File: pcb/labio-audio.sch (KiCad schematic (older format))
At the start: 32 parts, among them J701 JACK_TRRS_6PINS, P701 CONN_01X04, P702 CONN_01X04, P703 CONN_01X04, P704 CONN_01X02, SW701 DIP_SWITCH_X04, SW702 DIP_SWITCH_X04, U701 SPU0410HR5H, U702 WM8750

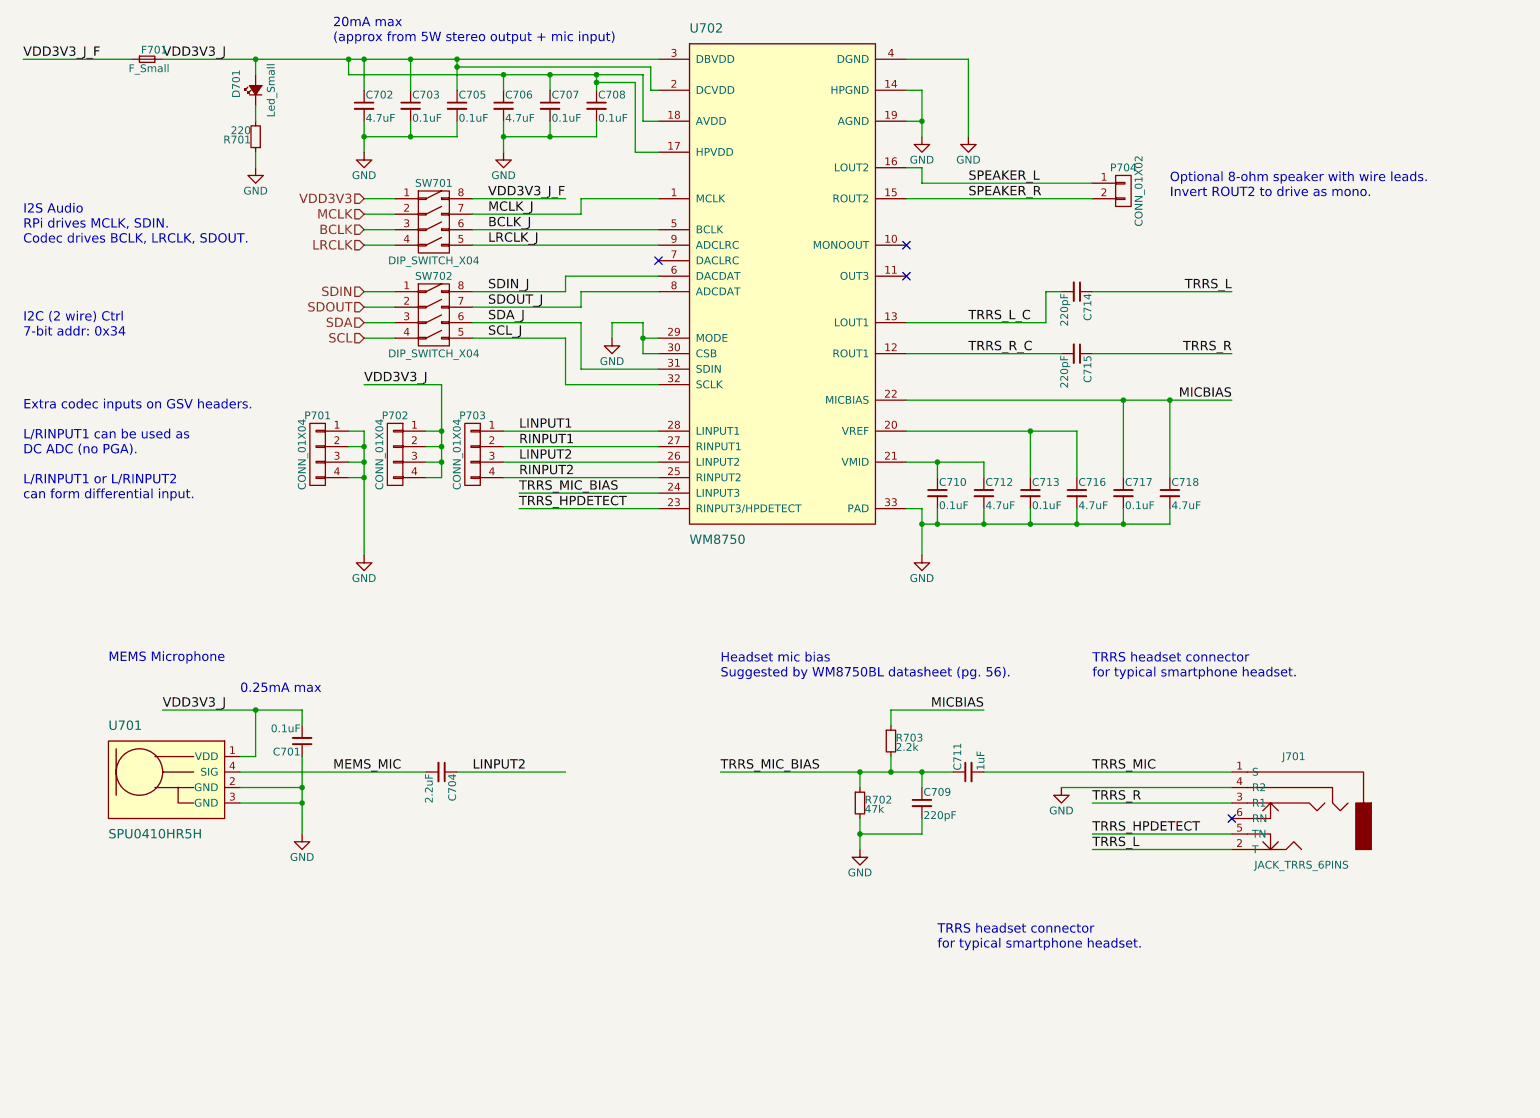
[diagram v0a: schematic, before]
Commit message: fix codec/mic/trrs bias circuit
* trrs (headset) mic bias was flipped (in vs out) from datasheet
* trrs l/r decoupling caps changed back to 220uF per datasheet and re-layout for 1210 ceramic
* mems mic decoupling changed to 1uF for consistency
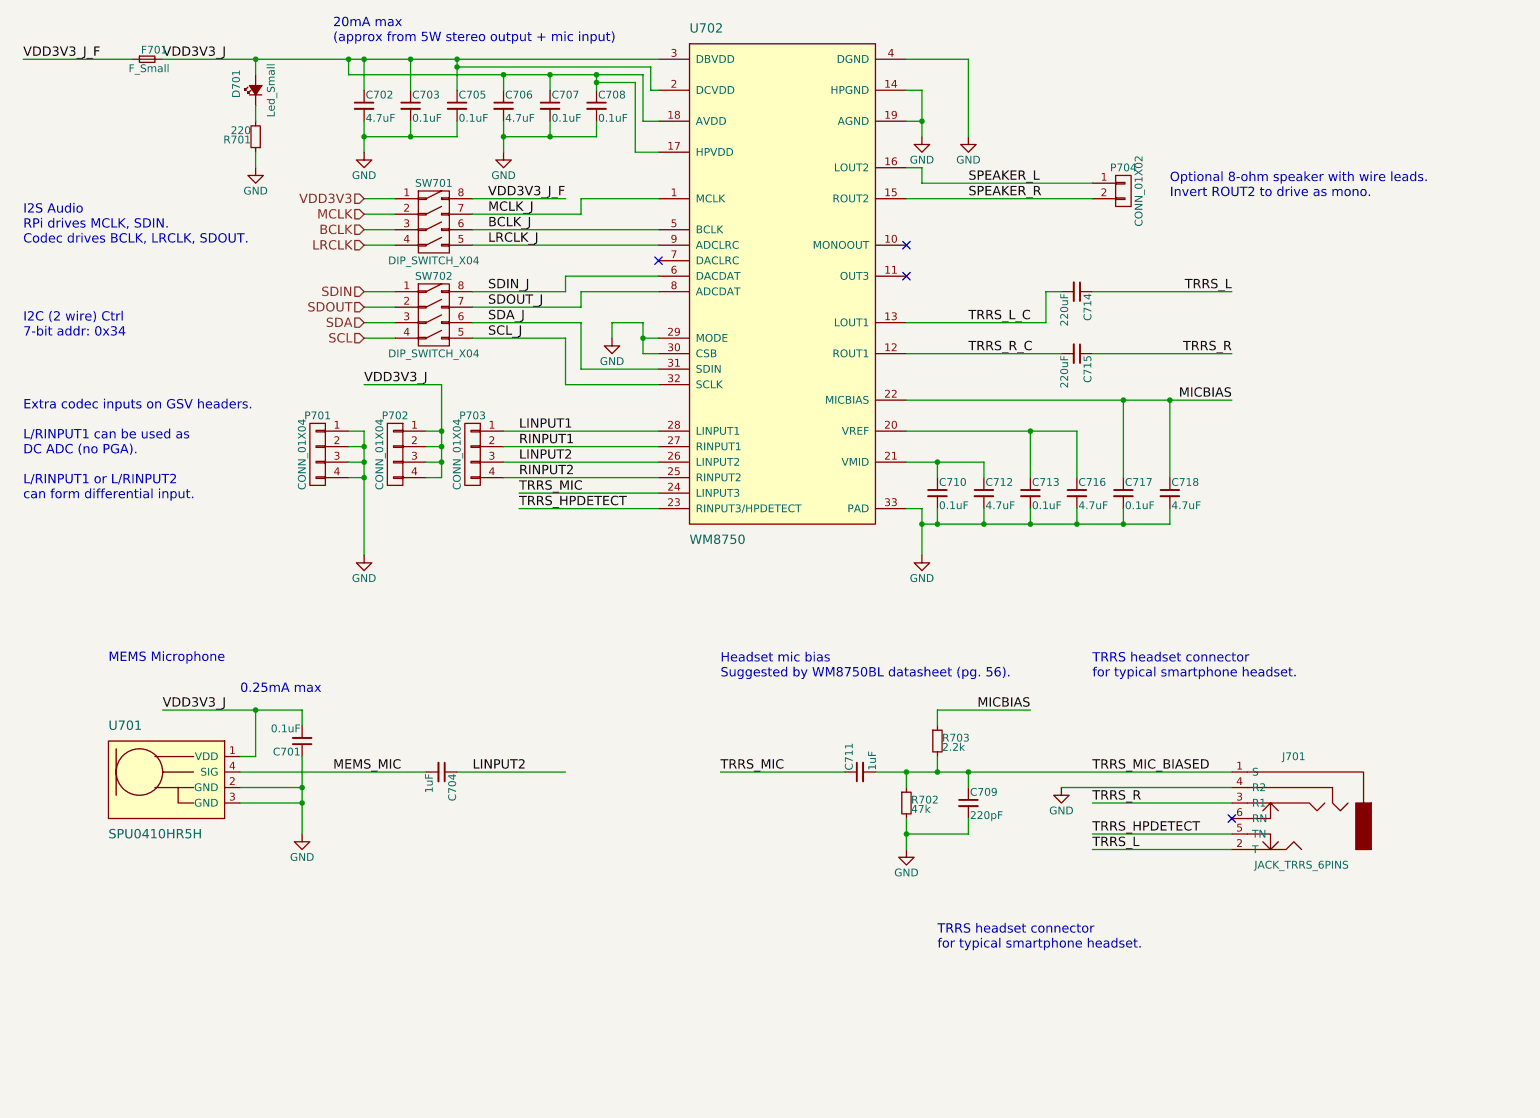
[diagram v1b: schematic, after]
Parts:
- C704: value 2.2uF -> 1uF
- C714, C715: value 220pF -> 220uF; footprint Capacitors_SMD:C_0603 -> Capacitors_SMD:C_1210
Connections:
- net TRRS_MIC: now also C711.1, U702.24 (LINPUT3); no longer C711.2, J701.1 (S)
- net TRRS_MIC_BIAS renamed TRRS_MIC_BIASED
- net TRRS_MIC_BIASED: now also C711.2, J701.1 (S); no longer C711.1, U702.24 (LINPUT3)
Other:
- moved on the sheet: C709, C711, R702, R703
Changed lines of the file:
@@
 $EndComp
-Wire Wire Line
-	7400 5600 9000 5600
 Wire Wire Line
 	9000 6000 8100 6000
 Text Label 8100 5600 0    60   ~ 0
-TRRS_MIC
+TRRS_MIC_BIASED
 Text Label 8100 6000 0    60   ~ 0
 TRRS_HPDETECT
@@
 TRRS_HPDETECT
 Text Label 4400 3800 0    60   ~ 0
-TRRS_MIC_BIAS
+TRRS_MIC
 $Comp
 L C_Small C715
@@
 P 8000 2900
 F 0 "C715" H 8010 2970 50  0000 L CNN
-F 1 "220pF" H 8010 2820 50  0000 L CNN
-F 2 "Capacitors_SMD:C_0603" H 8000 2900 50  0001 C CNN
+F 1 "220uF" H 8010 2820 50  0000 L CNN
+F 2 "Capacitors_SMD:C_1210" H 8000 2900 50  0001 C CNN
 F 3 "" H 8000 2900 50  0000 C CNN
 	1    8000 2900
@@
 P 8000 2500
 F 0 "C714" H 8010 2570 50  0000 L CNN
-F 1 "220pF" H 8010 2420 50  0000 L CNN
-F 2 "Capacitors_SMD:C_0603" H 8000 2500 50  0001 C CNN
+F 1 "220uF" H 8010 2420 50  0000 L CNN
+F 2 "Capacitors_SMD:C_1210" H 8000 2500 50  0001 C CNN
 F 3 "" H 8000 2500 50  0000 C CNN
 	1    8000 2500
@@
 P 3900 5600
 F 0 "C704" H 3910 5670 50  0000 L CNN
-F 1 "2.2uF" H 3910 5520 50  0000 L CNN
+F 1 "1uF" H 3910 5520 50  0000 L CNN
 F 2 "Capacitors_SMD:C_0603" H 3900 5600 50  0001 C CNN
 F 3 "" H 3900 5600 50  0000 C CNN
@@
 L C_Small C709
 U 1 1 575C86CC
-P 7000 5800
-F 0 "C709" H 7010 5870 50  0000 L CNN
-F 1 "220pF" H 7010 5720 50  0000 L CNN
-F 2 "Capacitors_SMD:C_0603" H 7000 5800 50  0001 C CNN
-F 3 "" H 7000 5800 50  0000 C CNN
-	1    7000 5800
+P 7300 5800
+F 0 "C709" H 7310 5870 50  0000 L CNN
+F 1 "220pF" H 7310 5720 50  0000 L CNN
+F 2 "Capacitors_SMD:C_0603" H 7300 5800 50  0001 C CNN
+F 3 "" H 7300 5800 50  0000 C CNN
+	1    7300 5800
 	1    0    0    -1
 $EndComp
@@
 L C_Small C711
 U 1 1 575C8733
-P 7300 5600
-F 0 "C711" H 7310 5670 50  0000 L CNN
-F 1 "1uF" H 7310 5520 50  0000 L CNN
-F 2 "Capacitors_SMD:C_0603" H 7300 5600 50  0001 C CNN
-F 3 "" H 7300 5600 50  0000 C CNN
-	1    7300 5600
+P 6600 5600
+F 0 "C711" H 6610 5670 50  0000 L CNN
+F 1 "1uF" H 6610 5520 50  0000 L CNN
+F 2 "Capacitors_SMD:C_0603" H 6600 5600 50  0001 C CNN
+F 3 "" H 6600 5600 50  0000 C CNN
+	1    6600 5600
 	0    -1   -1   0
 $EndComp
@@
 L R_Small R702
 U 1 1 575C8919
-P 6600 5800
-F 0 "R702" H 6630 5820 50  0000 L CNN
-F 1 "47k" H 6630 5760 50  0000 L CNN
-F 2 "Resistors_SMD:R_0603" H 6600 5800 50  0001 C CNN
-F 3 "" H 6600 5800 50  0000 C CNN
-	1    6600 5800
+P 6900 5800
+F 0 "R702" H 6930 5820 50  0000 L CNN
+F 1 "47k" H 6930 5760 50  0000 L CNN
+F 2 "Resistors_SMD:R_0603" H 6900 5800 50  0001 C CNN
+F 3 "" H 6900 5800 50  0000 C CNN
+	1    6900 5800
 	1    0    0    -1
 $EndComp
@@
 L R_Small R703
 U 1 1 575C8A55
-P 6800 5400
-F 0 "R703" H 6830 5420 50  0000 L CNN
-F 1 "2.2k" H 6830 5360 50  0000 L CNN
-F 2 "Resistors_SMD:R_0603" H 6800 5400 50  0001 C CNN
-F 3 "" H 6800 5400 50  0000 C CNN
-	1    6800 5400
-	1    0    0    -1
-$EndComp
-Wire Wire Line
-	6600 5700 6600 5600
-Wire Wire Line
-	5700 5600 7200 5600
-Connection ~ 6600 5600
-Wire Wire Line
-	7000 5700 7000 5600
-Connection ~ 7000 5600
-Wire Wire Line
-	6600 5900 6600 6100
-Wire Wire Line
-	6600 6000 7000 6000
-Wire Wire Line
-	7000 6000 7000 5900
-Connection ~ 6600 6000
-Wire Wire Line
-	6800 5300 6800 5200
-Wire Wire Line
-	6800 5200 7400 5200
-Text Label 7400 5200 2    60   ~ 0
+P 7100 5400
+F 0 "R703" H 7130 5420 50  0000 L CNN
+F 1 "2.2k" H 7130 5360 50  0000 L CNN
+F 2 "Resistors_SMD:R_0603" H 7100 5400 50  0001 C CNN
+F 3 "" H 7100 5400 50  0000 C CNN
+	1    7100 5400
+	1    0    0    -1
+$EndComp
+Wire Wire Line
+	6900 5700 6900 5600
+Connection ~ 6900 5600
+Wire Wire Line
+	7300 5600 7300 5700
+Connection ~ 7300 5600
+Wire Wire Line
+	6900 5900 6900 6100
+Wire Wire Line
+	6900 6000 7300 6000
+Wire Wire Line
+	7300 6000 7300 5900
+Connection ~ 6900 6000
+Wire Wire Line
+	7100 5300 7100 5200
+Wire Wire Line
+	7100 5200 7700 5200
+Text Label 7700 5200 2    60   ~ 0
 MICBIAS
 Text Label 5700 5600 0    60   ~ 0
-TRRS_MIC_BIAS
-Wire Wire Line
-	6800 5500 6800 5600
-Connection ~ 6800 5600
+TRRS_MIC
+Wire Wire Line
+	7100 5600 7100 5500
+Connection ~ 7100 5600
 Text Notes 5700 5000 0    60   ~ 0
 Headset mic bias\nSuggested by WM8750BL datasheet (pg. 56).
@@
 L GND #PWR049
 U 1 1 578E32B4
-P 6600 6100
-F 0 "#PWR049" H 6600 5850 50  0001 C CNN
-F 1 "GND" H 6600 5950 50  0000 C CNN
-F 2 "" H 6600 6100 50  0000 C CNN
-F 3 "" H 6600 6100 50  0000 C CNN
-	1    6600 6100
+P 6900 6100
+F 0 "#PWR049" H 6900 5850 50  0001 C CNN
+F 1 "GND" H 6900 5950 50  0000 C CNN
+F 2 "" H 6900 6100 50  0000 C CNN
+F 3 "" H 6900 6100 50  0000 C CNN
+	1    6900 6100
 	1    0    0    -1
 $EndComp
@@
 Text Label 1200 1000 0    60   ~ 0
 VDD3V3_J_F
+Wire Wire Line
+	6700 5600 9000 5600
+Wire Wire Line
+	6500 5600 5700 5600
 $EndSCHEMATC

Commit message: Fix ADC reading mic, possible backpowering, encoder pull downs, vias in footprint:
* Mic needs on-board path to ADC. Add proper bias and amp. Connect to ADC or codec with switches.
* Mic footprint (U701) flipped. Redraw footprint and adjust routing.
* Remove power from dip switches and replace with fuses. Turning power off to a block could result in backpower from driven IO lines.
* Remove/adjust pull downs on LEDs for encoder/dpad lines.
* Move vias out of display connector (P401) footprint.
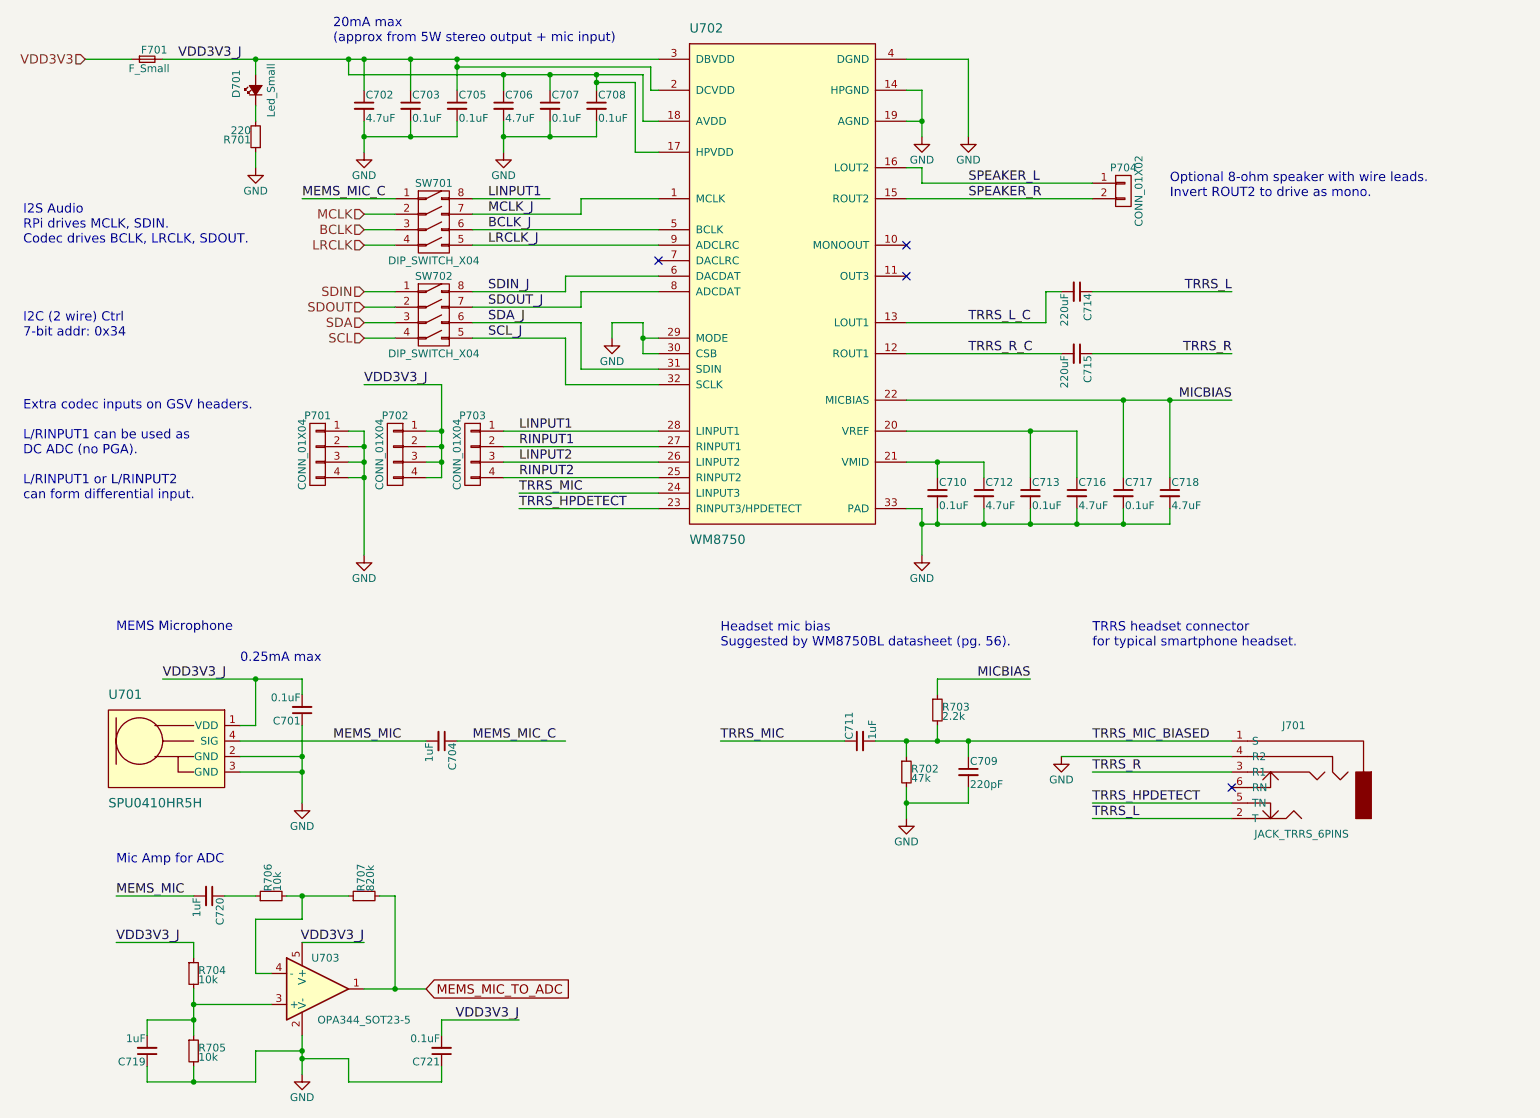
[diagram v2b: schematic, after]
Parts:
- added C719, C720: 1uF, Capacitors_SMD:C_0603, symbol C_Small
- added C721: 0.1uF, Capacitors_SMD:C_0603, symbol C_Small
- added R704, R705, R706: 10k, Resistors_SMD:R_0603, symbol R_Small
- added R707: 820k, Resistors_SMD:R_0603, symbol R_Small
- added U703: OPA344_SOT23-5, TO_SOT_Packages_SMD:SOT-23-5, symbol OPA344_SOT23-5
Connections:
- net GND: now also C719.1, C721.1, R705.2, U703.2 (V-)
- net LINPUT1: now also SW701.8 (1B)
- net LINPUT2: no longer C704.1
- net MEMS_MIC: now also C720.2
- net VDD3V3: now also F701.1; no longer SW701.1 (1A)
- net VDD3V3_J: now also C721.2, R704.1, U703.5 (V+)
- removed net VDD3V3_J_F: F701.1, SW701.8 (1B)
- new net: C719.2, R704.2, R705.1, U703.3 (+)
- new net: R706.2, R707.1, U703.4 (-)
- new net: C720.1, R706.1
- new net MEMS_MIC_C: C704.1, SW701.1 (1A)
- new net MEMS_MIC_TO_ADC: R707.2, U703.1
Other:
- note added: "Mic Amp for ADC"
- moved on the sheet: C701, C704, C709, C711, J701, R702, R703, U701

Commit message: Fix i2c addresses, pressure sensor footprint, consolidate BOM
* Schematic should list I2C addresses for accelerometer, gyro.
* Pressure sensor footprint (U502) has pins in the wrong order. Redraw footprint and adjust routing.
* Bump i2c and photodiode pullups to 2.2k
* Remove R505 near gyro
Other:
- note added: "I2C (2 wire) Ctrl\n7-bit addr: 0x1A (0011010)"
- note added: "I2S Audio\nRPi drives MCLK, SDIN.\nCodec drives BCLK, LRCLK, SDOUT.\nWrite LRCM=1 to use ADCLRC as LRCLK."
- note removed: "I2C (2 wire) Ctrl\n7-bit addr: 0x34"
- note removed: "I2S Audio\nRPi drives MCLK, SDIN.\nCodec drives BCLK, LRCLK, SDOUT."
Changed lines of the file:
@@
 	4800 3000 5300 3000
 Text Notes 1200 2200 0    60   ~ 0
-I2S Audio\nRPi drives MCLK, SDIN.\nCodec drives BCLK, LRCLK, SDOUT.
+I2S Audio\nRPi drives MCLK, SDIN.\nCodec drives BCLK, LRCLK, SDOUT.\nWrite LRCM=1 to use ADCLRC as LRCLK.
 Text Notes 1200 2800 0    60   ~ 0
-I2C (2 wire) Ctrl\n7-bit addr: 0x34
+I2C (2 wire) Ctrl\n7-bit addr: 0x1A (0011010)
 Wire Wire Line
 	4700 2400 5300 2400
